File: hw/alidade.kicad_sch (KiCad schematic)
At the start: 0 parts

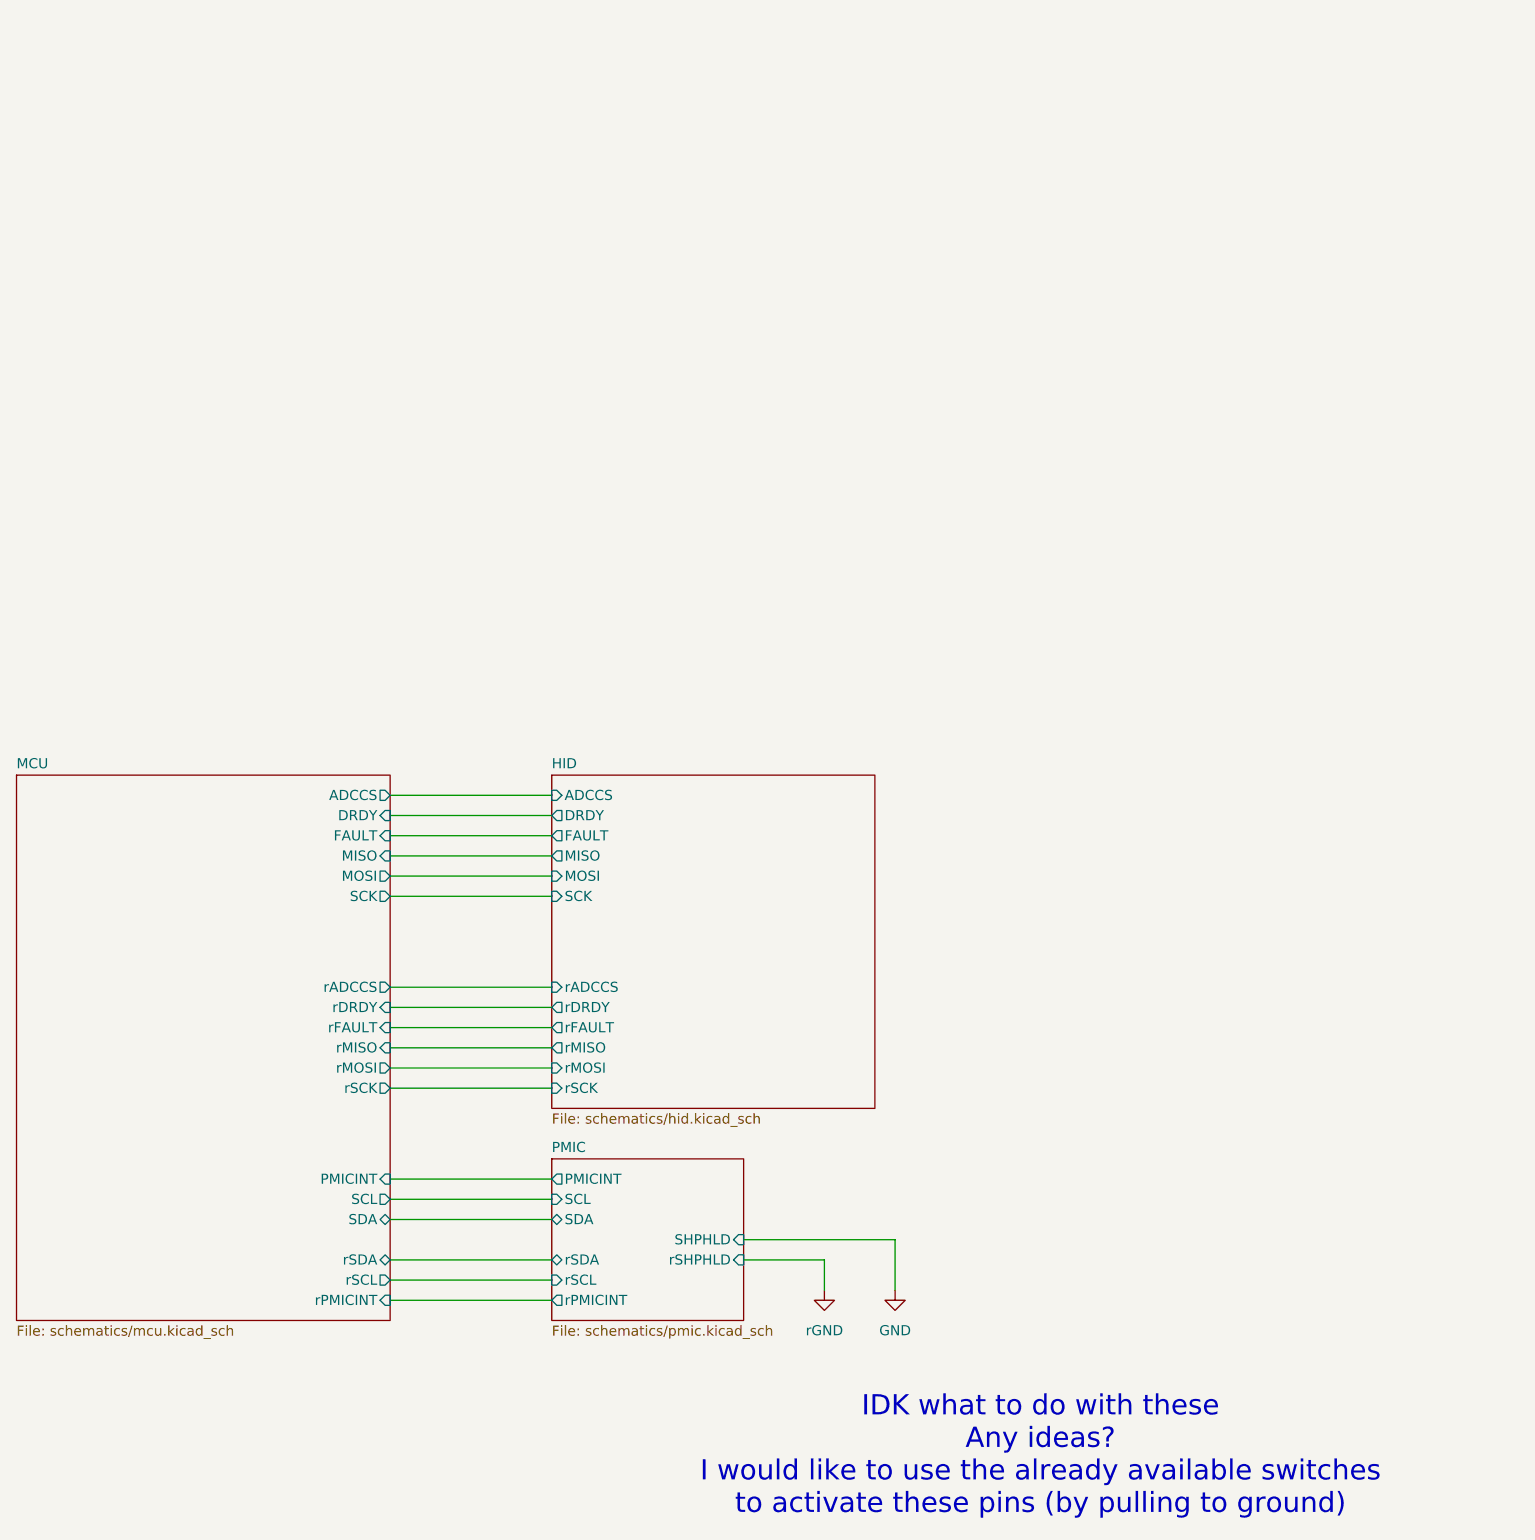
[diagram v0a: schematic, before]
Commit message: Hook up matrix
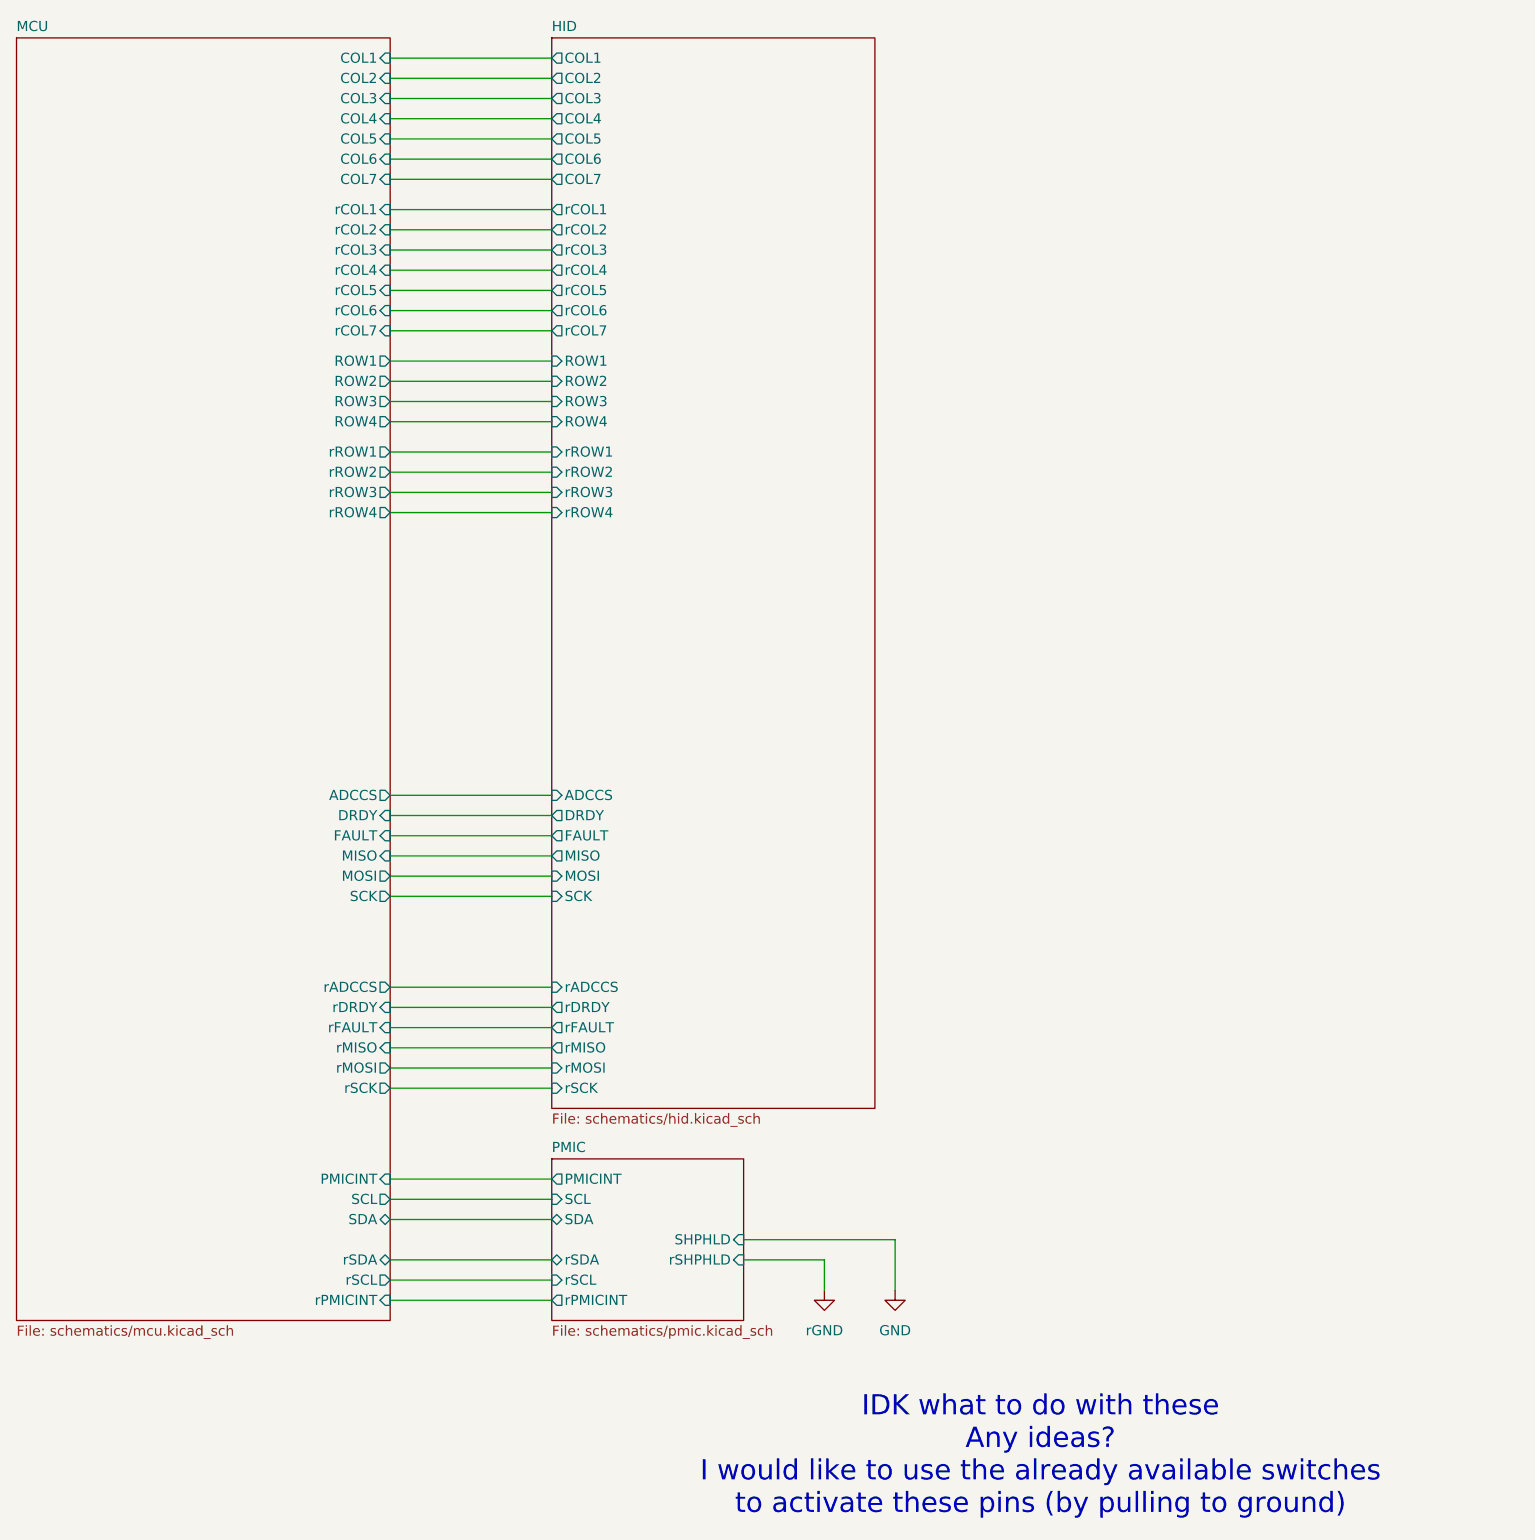
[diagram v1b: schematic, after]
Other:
- sheet HID ports: added COL1, COL2, COL3, COL4, COL5, COL6, COL7, ROW1, ROW2, ROW3, ROW4, rCOL1, rCOL2, rCOL3, rCOL4, rCOL5, rCOL6, rCOL7, rROW1, rROW2, rROW3, rROW4; removed none
- sheet MCU ports: added COL1, COL2, COL3, COL4, COL5, COL6, COL7, ROW1, ROW2, ROW3, ROW4, rCOL1, rCOL2, rCOL3, rCOL4, rCOL5, rCOL6, rCOL7, rROW1, rROW2, rROW3, rROW4; removed none

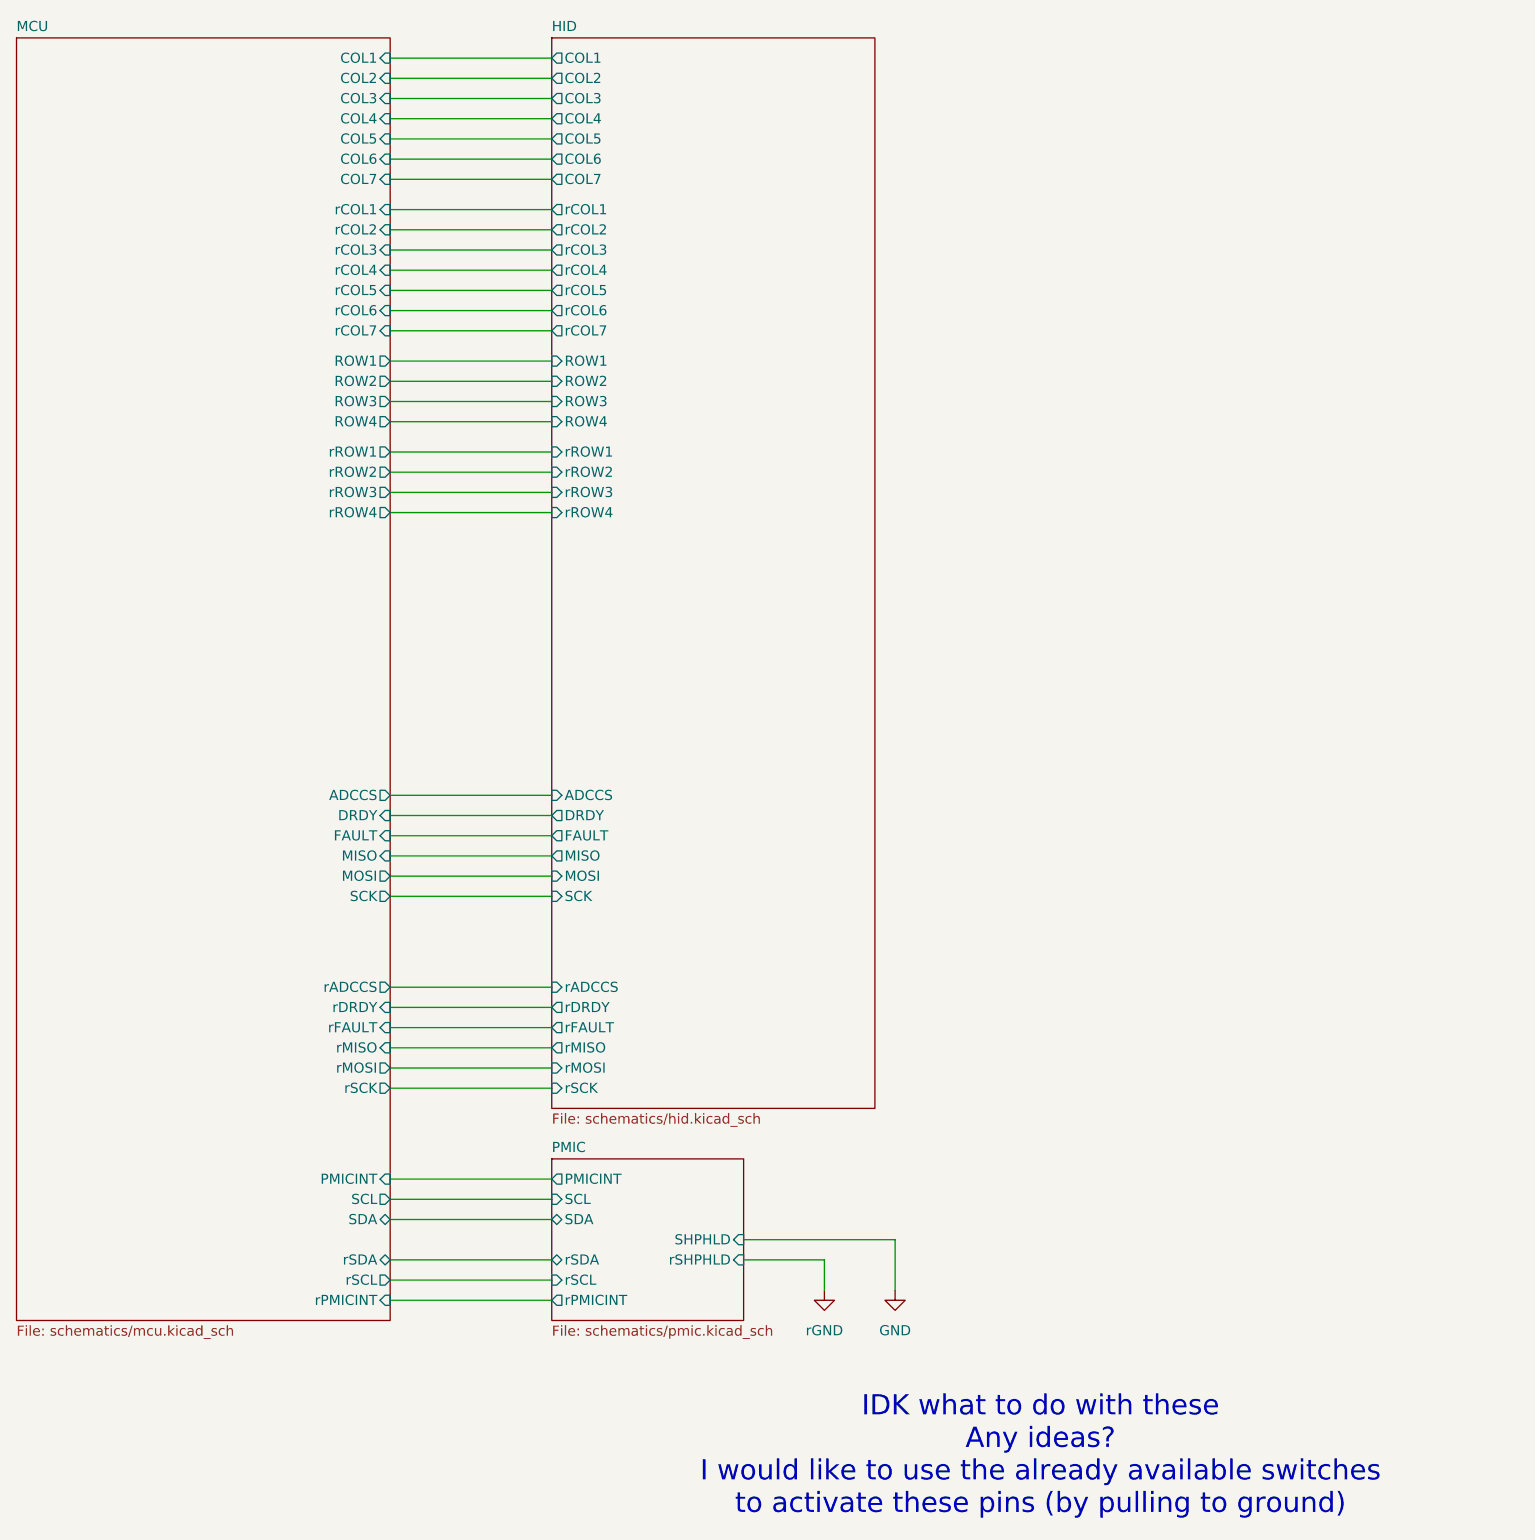
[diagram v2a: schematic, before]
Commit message: Place shphld switches
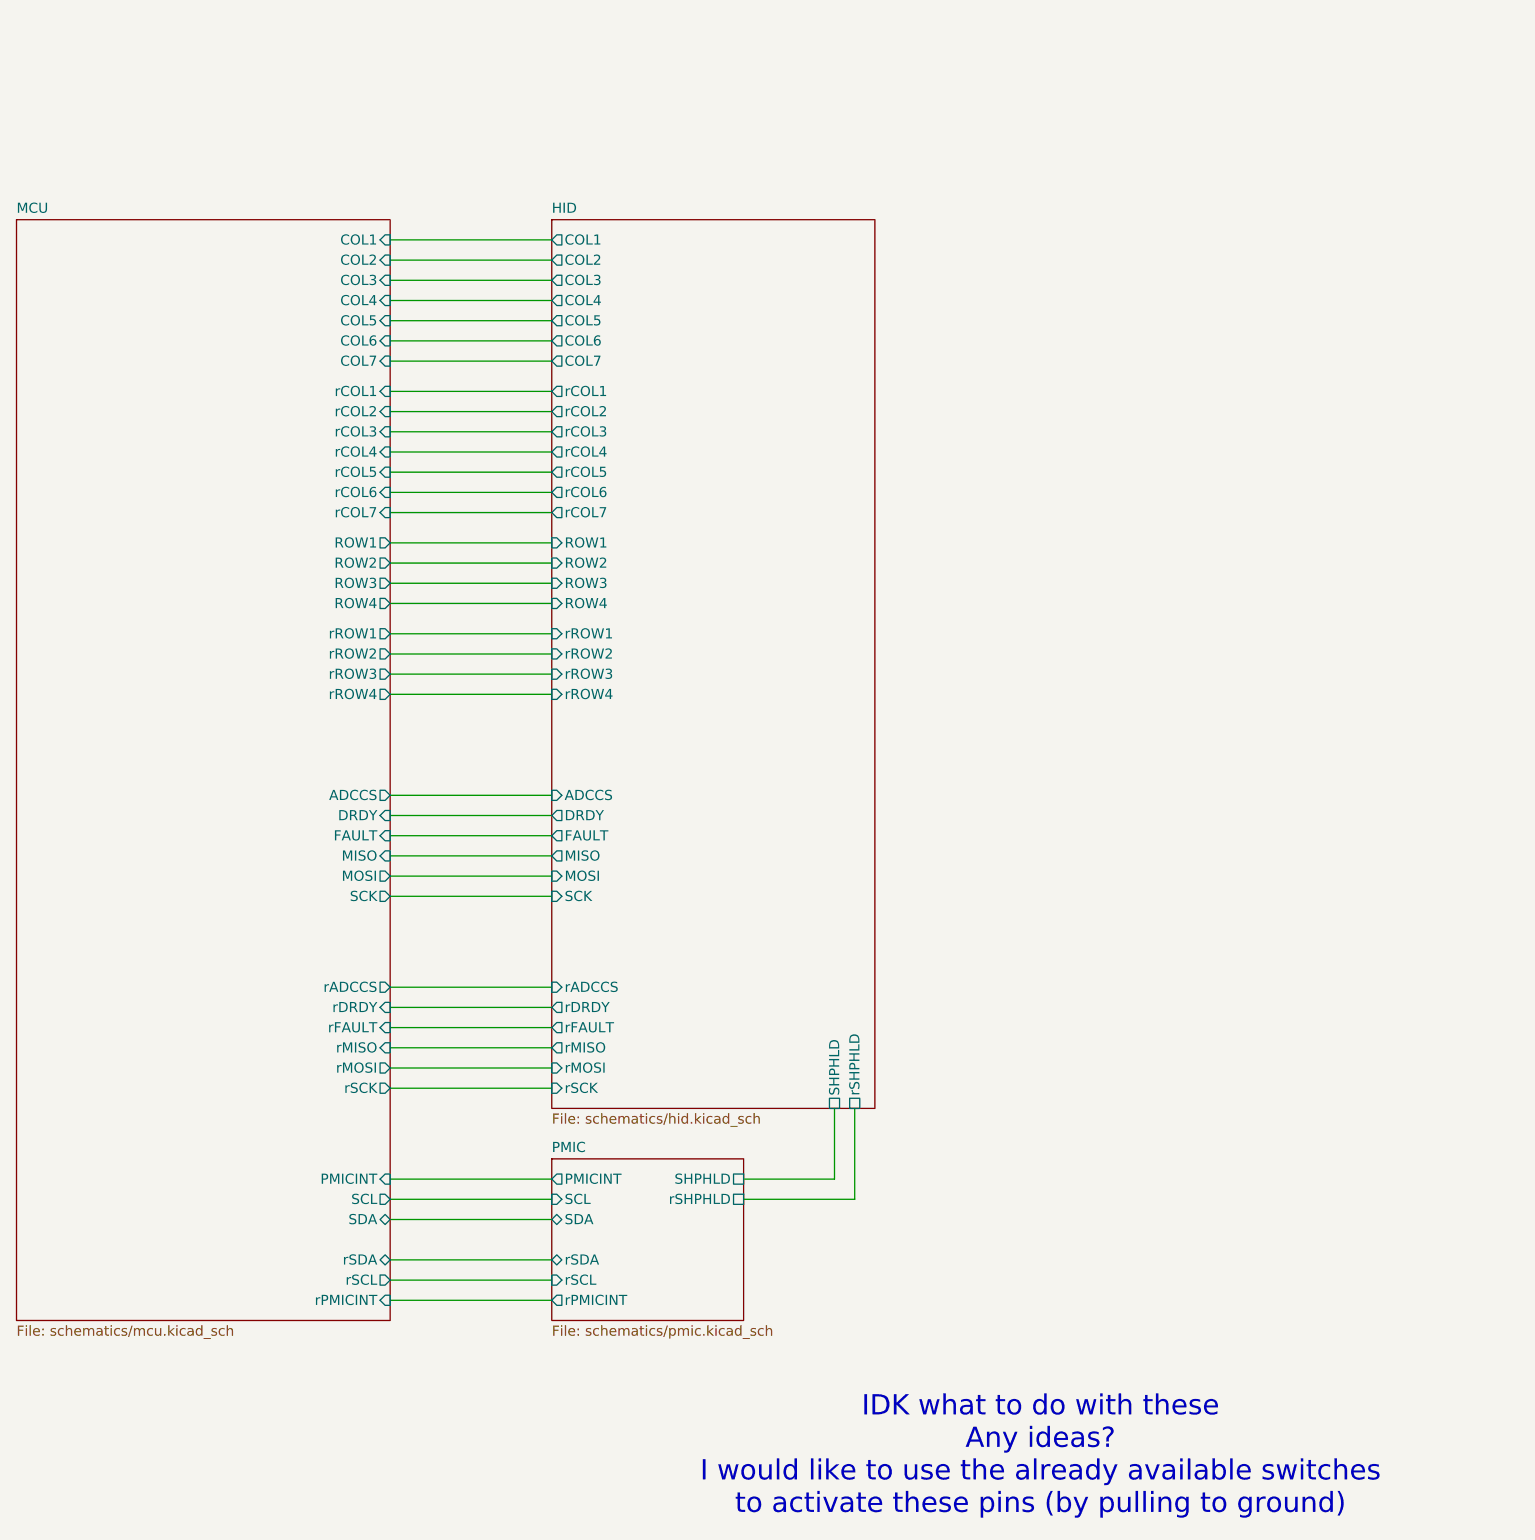
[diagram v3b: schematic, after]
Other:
- sheet HID ports: added SHPHLD, rSHPHLD; removed none
